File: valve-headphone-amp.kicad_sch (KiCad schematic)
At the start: 48 parts

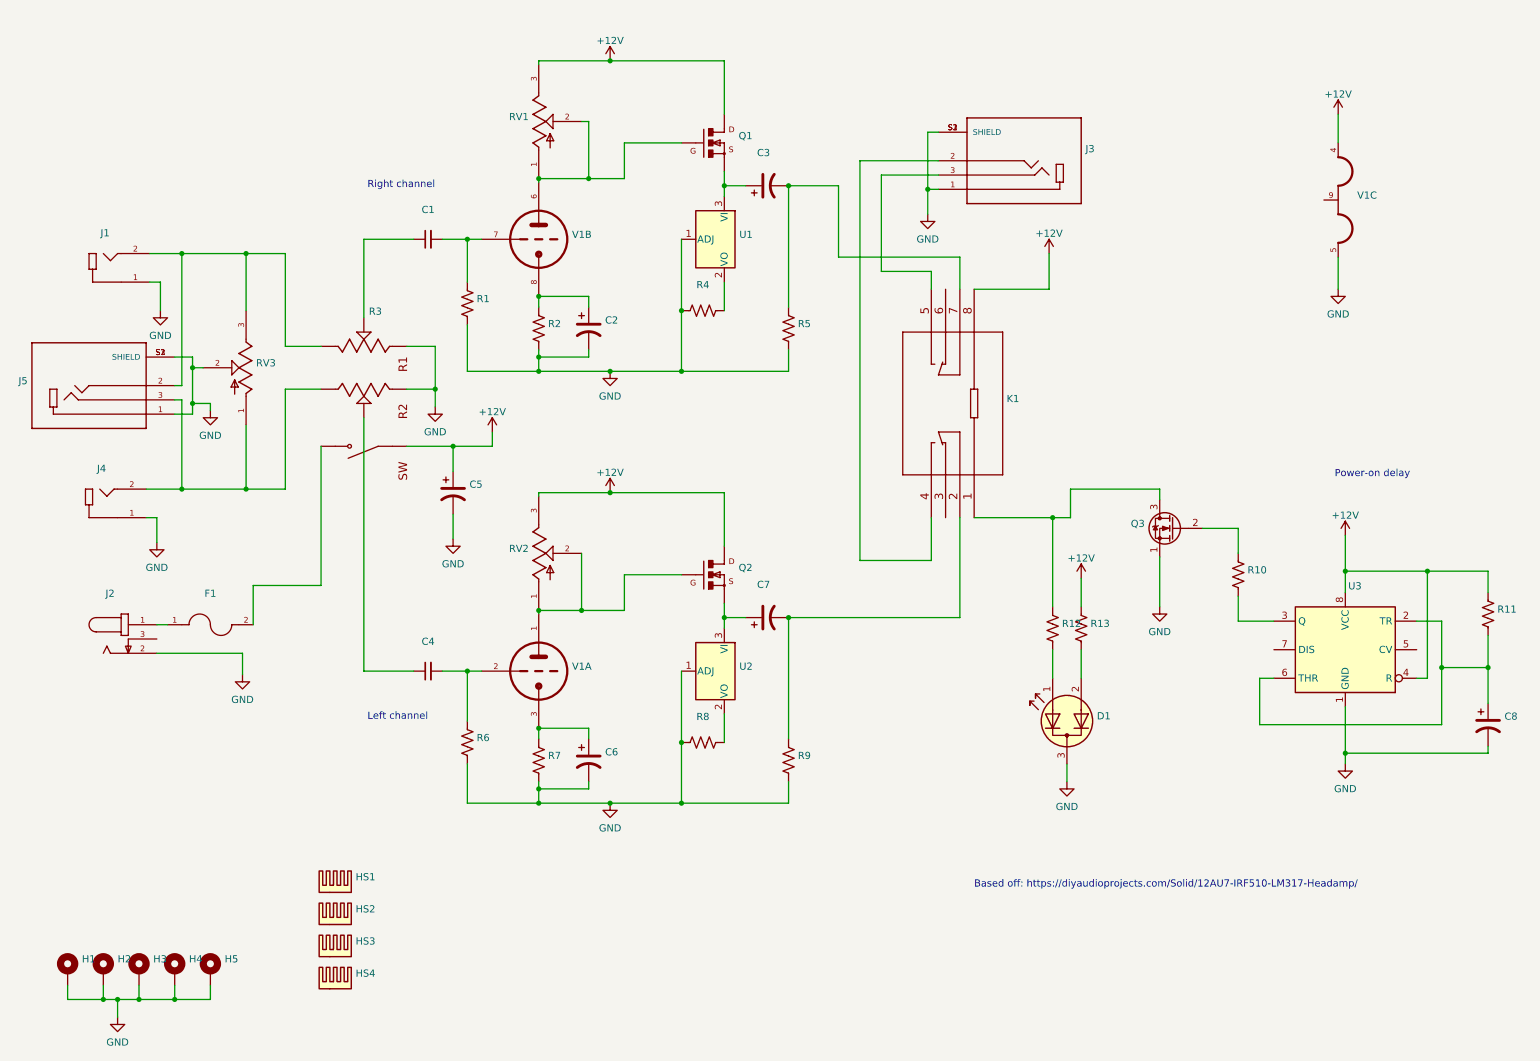
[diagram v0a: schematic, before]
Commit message: Version with TRRS and media button support
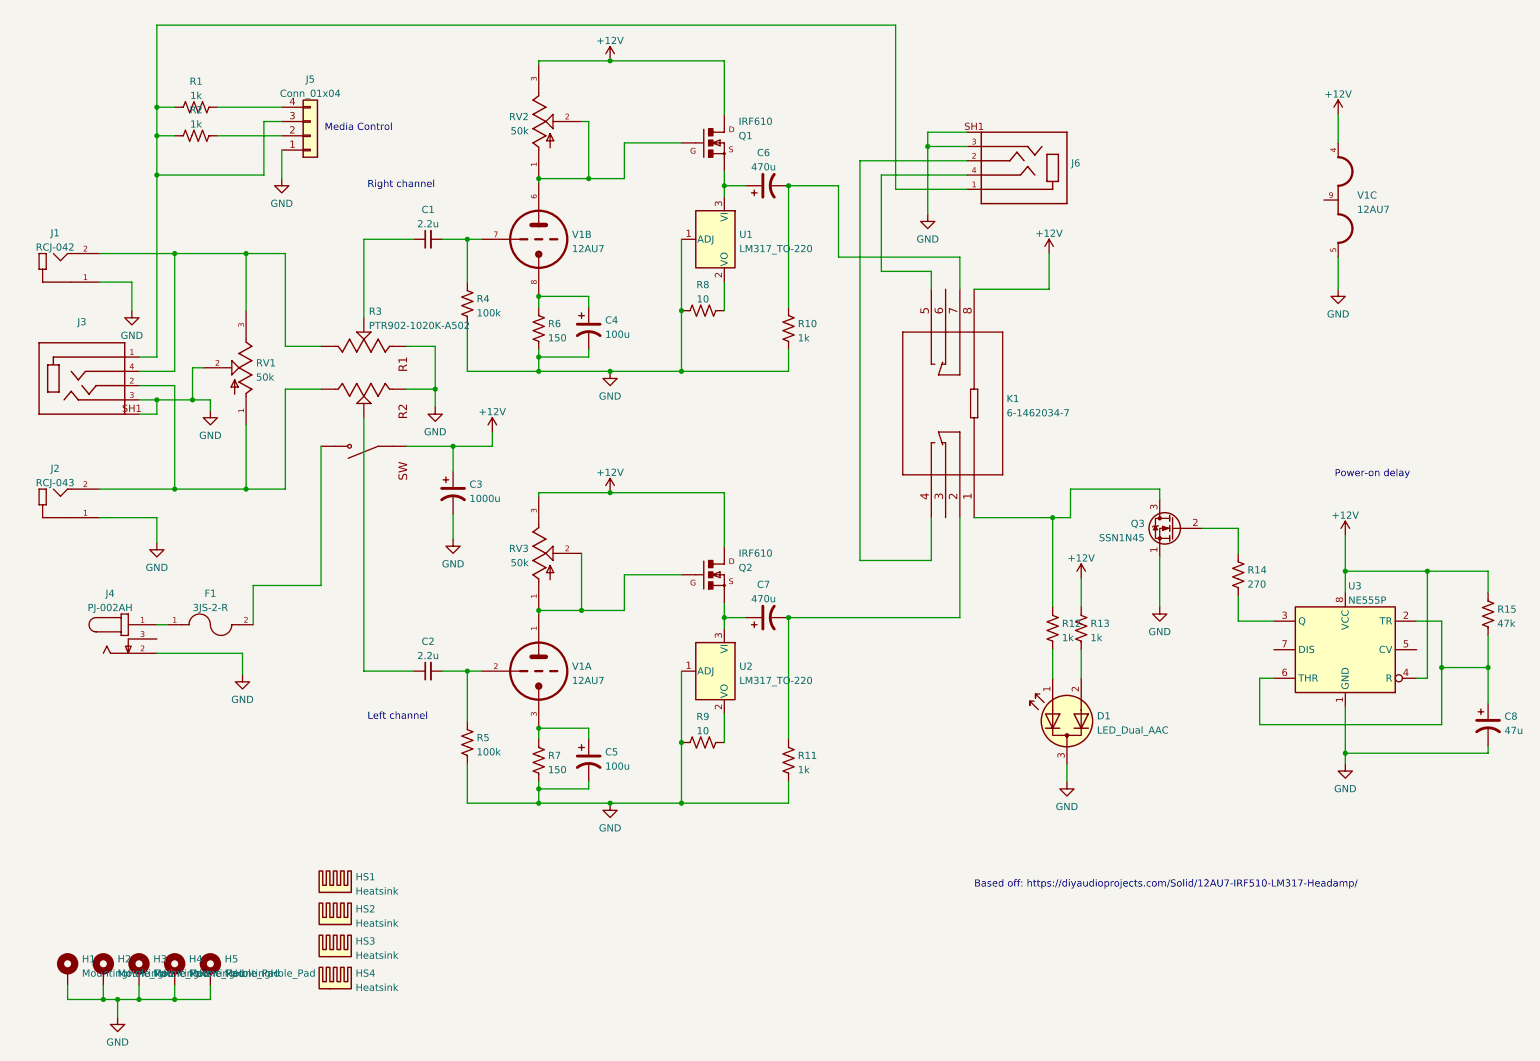
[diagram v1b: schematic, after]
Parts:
- removed J3, J5: (no value), symbol SJ1-3533NS:SJ1-3533NS
- added J3, J6: (no value), CUI_SJ-435107, symbol SJ-435107:SJ-435107
- added J5: Conn_01x04, Connector_PinHeader_2.54mm:PinHeader_1x04_P2.54mm_Vertical, symbol Connector_Generic:Conn_01x04
- added R1, R2: 1k, Resistor_THT:R_Axial_DIN0309_L9.0mm_D3.2mm_P12.70mm_Horizontal, symbol Device:R_US
- C1: value (none) -> 2.2u; footprint (none) -> Capacitor_THT:C_Rect_L7.2mm_W5.5mm_P5.00mm_FKS2_FKP2_MKS2_MKP2
- C2: renamed from C4; value (none) -> 2.2u; footprint (none) -> Capacitor_THT:C_Rect_L7.2mm_W5.5mm_P5.00mm_FKS2_FKP2_MKS2_MKP2
- C3: renamed from C5; value (none) -> 1000u; footprint (none) -> w_capacitors:CP_10x20mm_horiz-L
- C4: renamed from C2; value (none) -> 100u; footprint (none) -> rubycon:25ZL100MEFCT16.3X11
- C5: renamed from C6; value (none) -> 100u; footprint (none) -> rubycon:25ZL100MEFCT16.3X11
- C6: renamed from C3; value (none) -> 470u; footprint (none) -> Capacitor_THT:CP_Radial_D10.0mm_P5.00mm
- C7: value (none) -> 470u; footprint (none) -> Capacitor_THT:CP_Radial_D10.0mm_P5.00mm
- C8: value (none) -> 47u; footprint (none) -> Capacitor_THT:CP_Radial_D5.0mm_P2.50mm
- D1: value (none) -> LED_Dual_AAC; footprint (none) -> LED_THT:LED_D3.0mm-3
- F1: value (none) -> 3JS-2-R; footprint (none) -> fuses:3JS 1-R
- H1, H2, H3, H4, H5: value (none) -> MountingHole_Pad; footprint (none) -> MountingHole:MountingHole_3.2mm_M3_Pad_Via
- HS1, HS2, HS3, HS4: value (none) -> Heatsink; footprint (none) -> heatsink:heatsink_19x13mm
- J1: value (none) -> RCJ-042; footprint (none) -> rca:CUI_RCJ-042
- J2: renamed from J4; value (none) -> RCJ-043; footprint (none) -> rca:CUI_RCJ-043
- J4: renamed from J2; value (none) -> PJ-002AH; footprint (none) -> power:CUI_PJ-002AH
- K1: value (none) -> 6-1462034-7; footprint (none) -> footprints:PC323-12L-X
- Q1, Q2: value (none) -> IRF610; footprint (none) -> Package_TO_SOT_THT:TO-220-3_Horizontal_TabDown
- Q3: value (none) -> SSN1N45; footprint (none) -> Package_TO_SOT_THT:TO-92_Inline_Wide
- R10: renamed from R5; value (none) -> 1k; footprint (none) -> Resistor_THT:R_Axial_DIN0309_L9.0mm_D3.2mm_P12.70mm_Horizontal
- R11: renamed from R9; value (none) -> 1k; footprint (none) -> Resistor_THT:R_Axial_DIN0309_L9.0mm_D3.2mm_P12.70mm_Horizontal
- R12, R13: value (none) -> 1k; footprint (none) -> Resistor_THT:R_Axial_DIN0309_L9.0mm_D3.2mm_P12.70mm_Horizontal
- R14: renamed from R10; value (none) -> 270; footprint (none) -> Resistor_THT:R_Axial_DIN0309_L9.0mm_D3.2mm_P12.70mm_Horizontal
- R15: renamed from R11; value (none) -> 47k; footprint (none) -> Resistor_THT:R_Axial_DIN0309_L9.0mm_D3.2mm_P12.70mm_Horizontal
- R3: value (none) -> PTR902-1020K-A502; footprint (none) -> pot:TRIM_PTR902-1020K-A502
- R4: renamed from R1; value (none) -> 100k; footprint (none) -> Resistor_THT:R_Axial_DIN0309_L9.0mm_D3.2mm_P12.70mm_Horizontal
- R5: renamed from R6; value (none) -> 100k; footprint (none) -> Resistor_THT:R_Axial_DIN0309_L9.0mm_D3.2mm_P12.70mm_Horizontal
- R6: renamed from R2; value (none) -> 150; footprint (none) -> Resistor_THT:R_Axial_DIN0309_L9.0mm_D3.2mm_P12.70mm_Horizontal
- R7: value (none) -> 150; footprint (none) -> Resistor_THT:R_Axial_DIN0309_L9.0mm_D3.2mm_P12.70mm_Horizontal
- R8: renamed from R4; value (none) -> 10; footprint (none) -> Resistor_THT:R_Axial_DIN0309_L9.0mm_D3.2mm_P12.70mm_Horizontal
- R9: renamed from R8; value (none) -> 10; footprint (none) -> Resistor_THT:R_Axial_DIN0309_L9.0mm_D3.2mm_P12.70mm_Horizontal
- RV1: renamed from RV3; value (none) -> 50k; footprint (none) -> Potentiometer_THT:Potentiometer_Bourns_3296W_Vertical
- RV2: renamed from RV1; value (none) -> 50k; footprint (none) -> Potentiometer_THT:Potentiometer_Bourns_3296W_Vertical
- RV3: renamed from RV2; value (none) -> 50k; footprint (none) -> Potentiometer_THT:Potentiometer_Bourns_3296W_Vertical
- U1, U2: value (none) -> LM317_TO-220; footprint (none) -> Package_TO_SOT_THT:TO-220-3_Horizontal_TabDown
- U3: value (none) -> NE555P; footprint (none) -> Package_DIP:DIP-8_W7.62mm
- V1: value (none) -> 12AU7; footprint (none) -> 12au7:socket_gzc9-b
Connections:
- net GND: now also J3.3, J3.SH1 (Shield), J5.1 (Pin_1), J6.3, J6.SH1 (Shield)
- net at J1.2, R3.R1_3, RV1.3: now also J3.4
- net at J2.2, R3.R2_3, RV1.1: now also J3.2
- net at K1.4: now also J6.2
- net at K1.5: now also J6.4
- new net: J3.1, J5.3 (Pin_3), J6.1, R1.2, R2.2
- new net: J5.2 (Pin_2), R2.1
- new net: J5.4 (Pin_4), R1.1
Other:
- note added: "Media Control"
- moved on the sheet: J1, J2

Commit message: updates
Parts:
- added J4: (no value), symbol Connector_Generic:Conn_01x02
- J3: value (none) -> SJ-435107; footprint CUI_SJ-435107 -> (none)
- J7: renamed from J6; value (none) -> SJ-435107; footprint CUI_SJ-435107 -> (none)
- R1: value 1k -> (none)
- R2: value 1k -> (none); footprint Resistor_THT:R_Axial_DIN0309_L9.0mm_D3.2mm_P12.70mm_Horizontal -> (none)
- renumbered J4 to J5, J5 to J6
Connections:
- net at J3.1, J6.3 (Pin_3), R1.2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: now also J4.1 (Pin_1); no longer J7.1
- new net: J4.2 (Pin_2), J7.1
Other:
- note added: "Control Passthru"
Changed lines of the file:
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@@
+    (stroke (width 0) (type default) (color 0 0 0 0))
+  )
+  (wire (pts (xy 34.925 23.495) (xy 34.925 31.75))
     (stroke (width 0) (type default) (color 0 0 0 0))
   )
@@
     (stroke (width 0) (type default) (color 0 0 0 0))
   )
-  (wire (pts (xy 34.925 17.145) (xy 34.925 31.75))
+  (wire (pts (xy 34.925 17.145) (xy 34.925 20.955))
     (stroke (width 0) (type default) (color 0 0 0 0))
   )
@@
   )
   (text "Right channel" (at 72.39 46.355 0)
+    (effects (font (size 1.27 1.27)) (justify left bottom))
+  )
+  (text "Control\nPassthru" (at 19.05 24.13 0)
     (effects (font (size 1.27 1.27)) (justify left bottom))
   )
@@
   (symbol (lib_id "SJ-435107:SJ-435107") (at 189.23 41.275 180) (unit 1)
     (in_bom yes) (on_board yes) (fields_autoplaced)
-    (property "Reference" "J6" (id 0) (at 197.612 41.7103 0)
+    (property "Reference" "J7" (id 0) (at 197.612 41.7103 0)
       (effects (font (size 1.27 1.27)) (justify right))
     )
-    (property "Value" "" (id 1) (at 197.612 44.2472 0)
+    (property "Value" "SJ-435107" (id 1) (at 197.612 44.2472 0)
       (effects (font (size 1.27 1.27)) (justify right))
     )
-    (property "Footprint" "CUI_SJ-435107" (id 2) (at 189.23 41.275 0)
+    (property "Footprint" "" (id 2) (at 189.23 41.275 0)
       (effects (font (size 1.27 1.27)) (justify left bottom) hide)
     )
@@
   (symbol (lib_id "PJ-002AH:PJ-002AH") (at 29.845 126.365 0) (unit 1)
     (in_bom yes) (on_board yes) (fields_autoplaced)
-    (property "Reference" "J4" (id 0) (at 26.6065 118.271 0))
+    (property "Reference" "J5" (id 0) (at 26.6065 118.271 0))
     (property "Value" "PJ-002AH" (id 1) (at 26.6065 120.8079 0))
     (property "Footprint" "power:CUI_PJ-002AH" (id 2) (at 29.845 126.365 0)
@@
   (symbol (lib_id "Connector_Generic:Conn_01x04") (at 62.23 36.83 0) (mirror x) (unit 1)
     (in_bom yes) (on_board yes) (fields_autoplaced)
-    (property "Reference" "J5" (id 0) (at 62.23 26.7802 0))
+    (property "Reference" "J6" (id 0) (at 62.23 26.7802 0))
     (property "Value" "Conn_01x04" (id 1) (at 62.23 29.3171 0))
     (property "Footprint" "Connector_PinHeader_2.54mm:PinHeader_1x04_P2.54mm_Vertical" (id 2) (at 62.23 36.83 0)
@@
     (in_bom yes) (on_board yes) (fields_autoplaced)
     (property "Reference" "J3" (id 0) (at 21.59 69.9602 0))
-    (property "Value" "" (id 1) (at 21.59 72.4971 0))
-    (property "Footprint" "CUI_SJ-435107" (id 2) (at 21.59 81.28 0)
+    (property "Value" "SJ-435107" (id 1) (at 21.59 72.4971 0))
+    (property "Footprint" "" (id 2) (at 21.59 81.28 0)
       (effects (font (size 1.27 1.27)) (justify left bottom) hide)
     )
@@
     (pin "2")
     (pin "3")
+  )
+  (symbol (lib_id "Connector_Generic:Conn_01x02") (at 29.845 23.495 180) (unit 1)
+    (in_bom yes) (on_board yes) (fields_autoplaced)
+    (property "Reference" "J4" (id 0) (at 29.845 15.9852 0))
+    (property "Value" "" (id 1) (at 29.845 18.5221 0))
+    (property "Footprint" "" (id 2) (at 29.845 23.495 0)
+      (effects (font (size 1.27 1.27)) hide)
+    )
+    (property "Datasheet" "~" (id 3) (at 29.845 23.495 0)
+      (effects (font (size 1.27 1.27)) hide)
+    )
+    (pin "1")
+    (pin "2")
   )
   (symbol (lib_id "power:GND") (at 172.085 50.8 0) (unit 1)
@@
     (in_bom yes) (on_board yes) (fields_autoplaced)
     (property "Reference" "R1" (id 0) (at 41.91 27.1612 90))
-    (property "Value" "1k" (id 1) (at 41.91 29.6981 90))
+    (property "Value" "" (id 1) (at 41.91 29.6981 90))
     (property "Footprint" "Resistor_THT:R_Axial_DIN0309_L9.0mm_D3.2mm_P12.70mm_Horizontal" (id 2) (at 41.656 32.766 90)
       (effects (font (size 1.27 1.27)) hide)
@@
     (in_bom yes) (on_board yes) (fields_autoplaced)
     (property "Reference" "R2" (id 0) (at 41.91 32.2412 90))
-    (property "Value" "1k" (id 1) (at 41.91 34.7781 90))
-    (property "Footprint" "Resistor_THT:R_Axial_DIN0309_L9.0mm_D3.2mm_P12.70mm_Horizontal" (id 2) (at 41.656 37.846 90)
+    (property "Value" "" (id 1) (at 41.91 34.7781 90))
+    (property "Footprint" "" (id 2) (at 41.656 37.846 90)
       (effects (font (size 1.27 1.27)) hide)
     )
@@
     )
     (path "/84d9c043-c32e-4066-84c1-40ae49306f2c"
-      (reference "J3") (unit 1) (value "SJ-435107") (footprint "CUI_SJ-435107")
+      (reference "J3") (unit 1) (value "SJ-435107") (footprint "3:CUI_SJ-435107")
+    )
+    (path "/c0eb397c-0f0a-48f2-a4a7-a39c38857565"
+      (reference "J4") (unit 1) (value "Conn_01x02") (footprint "Connector_PinHeader_2.54mm:PinHeader_1x02_P2.54mm_Vertical")
     )
     (path "/53832443-1172-4109-a2d9-64535bfe1336"
-      (reference "J4") (unit 1) (value "PJ-002AH") (footprint "power:CUI_PJ-002AH")
+      (reference "J5") (unit 1) (value "PJ-002AH") (footprint "power:CUI_PJ-002AH")
     )
     (path "/73381ec2-87a3-49e2-98db-bb94bae0855b"
-      (reference "J5") (unit 1) (value "Conn_01x04") (footprint "Connector_PinHeader_2.54mm:PinHeader_1x04_P2.54mm_Vertical")
+      (reference "J6") (unit 1) (value "Conn_01x04") (footprint "Connector_PinHeader_2.54mm:PinHeader_1x04_P2.54mm_Vertical")
     )
     (path "/27105bf6-d25e-43b2-9995-951213911b71"
-      (reference "J6") (unit 1) (value "SJ-435107") (footprint "CUI_SJ-435107")
+      (reference "J7") (unit 1) (value "SJ-435107") (footprint "3:CUI_SJ-435107")
     )
     (path "/c4b8c9dd-daf6-4037-b6d3-bf98410c380c"
@@
     )
     (path "/ceb19b93-a3c8-47dc-a451-d369e61f83dc"
-      (reference "R1") (unit 1) (value "1k") (footprint "Resistor_THT:R_Axial_DIN0309_L9.0mm_D3.2mm_P12.70mm_Horizontal")
+      (reference "R1") (unit 1) (value "470") (footprint "Resistor_THT:R_Axial_DIN0309_L9.0mm_D3.2mm_P12.70mm_Horizontal")
     )
     (path "/efdaeac3-1e9e-4928-8703-9f2f703ecefd"
-      (reference "R2") (unit 1) (value "1k") (footprint "Resistor_THT:R_Axial_DIN0309_L9.0mm_D3.2mm_P12.70mm_Horizontal")
+      (reference "R2") (unit 1) (value "240") (footprint "Resistor_THT:R_Axial_DIN0309_L9.0mm_D3.2mm_P12.70mm_Horizontal")
     )
     (path "/6dd70f45-38b7-496b-a51c-7e8dcad7e8e2"

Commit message: updates, bom
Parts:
- C1, C2: value 2.2u -> (none); footprint Capacitor_THT:C_Rect_L7.2mm_W5.5mm_P5.00mm_FKS2_FKP2_MKS2_MKP2 -> (none)
- C3: value 1000u -> (none); footprint w_capacitors:CP_10x20mm_horiz-L -> (none)
- C4, C5: value 100u -> (none); footprint rubycon:25ZL100MEFCT16.3X11 -> (none)
- C6, C7: value 470u -> (none); footprint Capacitor_THT:CP_Radial_D10.0mm_P5.00mm -> (none)
- C8: value 47u -> (none); footprint Capacitor_THT:CP_Radial_D5.0mm_P2.50mm -> (none)
- D1: value LED_Dual_AAC -> (none); footprint LED_THT:LED_D3.0mm-3 -> (none)
- F1: value 3JS-2-R -> (none); footprint fuses:3JS 1-R -> (none)
- H1, H2, H3, H4, H5: value MountingHole_Pad -> (none); footprint MountingHole:MountingHole_3.2mm_M3_Pad_Via -> (none)
- HS1, HS2, HS3, HS4: value Heatsink -> (none); footprint heatsink:heatsink_19x13mm -> (none)
- J1: value RCJ-042 -> (none); footprint rca:CUI_RCJ-042 -> (none)
- J2: value RCJ-043 -> (none); footprint rca:CUI_RCJ-043 -> (none)
- J3, J7: value SJ-435107 -> (none); SUPPLIER_URL (none) -> https://www.digikey.com.au/en/products/detail/cui-devices/S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
- J5: value PJ-002AH -> (none); footprint power:CUI_PJ-002AH -> (none)
- J6: value Conn_01x04 -> (none); footprint Connector_PinHeader_2.54mm:PinHeader_1x04_P2.54mm_Vertical -> (none)
- K1: value 6-1462034-7 -> (none); footprint footprints:PC323-12L-X -> (none)
- Q1, Q2: value IRF610 -> (none); footprint Package_TO_SOT_THT:TO-220-3_Horizontal_TabDown -> (none)
- Q3: value SSN1N45 -> (none); footprint Package_TO_SOT_THT:TO-92_Inline_Wide -> (none)
- R1: footprint Resistor_THT:R_Axial_DIN0309_L9.0mm_D3.2mm_P12.70mm_Horizontal -> (none); PRICE (none) -> 0.32; SUPPLIER_URL https://www.digikey.com.au/en/products/detail/vishay-beyschlag-draloric-bc-components/SFR2500001001FR500/595699 -> https://www.digikey.com.au/en/products/detail/vishay-beyschlag-draloric-bc-components/SFR2500004700FR500/333902
- R10, R11, R12, R13: value 1k -> (none); footprint Resistor_THT:R_Axial_DIN0309_L9.0mm_D3.2mm_P12.70mm_Horizontal -> (none); PRICE (none) -> 0.20
- R14: value 270 -> (none); footprint Resistor_THT:R_Axial_DIN0309_L9.0mm_D3.2mm_P12.70mm_Horizontal -> (none); PRICE (none) -> 0.37; SUPPLIER_URL (none) -> https://www.digikey.com.au/en/products/detail/vishay-beysch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
- R15: value 47k -> (none); footprint Resistor_THT:R_Axial_DIN0309_L9.0mm_D3.2mm_P12.70mm_Horizontal -> (none); PRICE (none) -> 0.29; SUPPLIER_URL (none) -> https://www.digikey.com.au/en/products/detail/vishay-beysch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
- R2: PRICE (none) -> 0.37; SUPPLIER_URL https://www.digikey.com.au/en/products/detail/vishay-beyschlag-draloric-bc-components/SFR2500001001FR500/595699 -> https://www.digikey.com.au/en/products/detail/vishay-beyschlag-draloric-bc-components/MBA02040C2400FCT00/5062453
- R3: value PTR902-1020K-A502 -> (none); footprint pot:TRIM_PTR902-1020K-A502 -> (none)
- R4, R5: value 100k -> (none); footprint Resistor_THT:R_Axial_DIN0309_L9.0mm_D3.2mm_P12.70mm_Horizontal -> (none)
- R6, R7: value 150 -> (none); footprint Resistor_THT:R_Axial_DIN0309_L9.0mm_D3.2mm_P12.70mm_Horizontal -> (none)
- R8, R9: value 10 -> (none); footprint Resistor_THT:R_Axial_DIN0309_L9.0mm_D3.2mm_P12.70mm_Horizontal -> (none)
- RV1, RV2, RV3: value 50k -> (none); footprint Potentiometer_THT:Potentiometer_Bourns_3296W_Vertical -> (none); SUPPLIER_URL https://www.ebay.com.au/itm/165184663837 -> https://www.ebay.com.au/itm/151504157376
- U1, U2: value LM317_TO-220 -> (none); footprint Package_TO_SOT_THT:TO-220-3_Horizontal_TabDown -> (none)
- U3: value NE555P -> (none); footprint Package_DIP:DIP-8_W7.62mm -> (none); PRICE (none) -> 0.73; SUPPLIER_URL (none) -> https://www.digikey.com.au/en/products/detail/texas-instrum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
- V1: value 12AU7 -> (none); footprint 12au7:socket_gzc9-b -> (none)
